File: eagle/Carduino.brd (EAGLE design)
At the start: 92.5 x 92.5 mm, 81 parts, among them IC1 DS3231M+TRL, IC2 FT232RL, IC3 SN74HCS596DR, IC4 SN74HCS596DR, IC5 SN74HCS596DR, IC6 SN74HCS596DR, IC8 ATTINY404-SSNR, U1 BAT-HLD-012-SMT

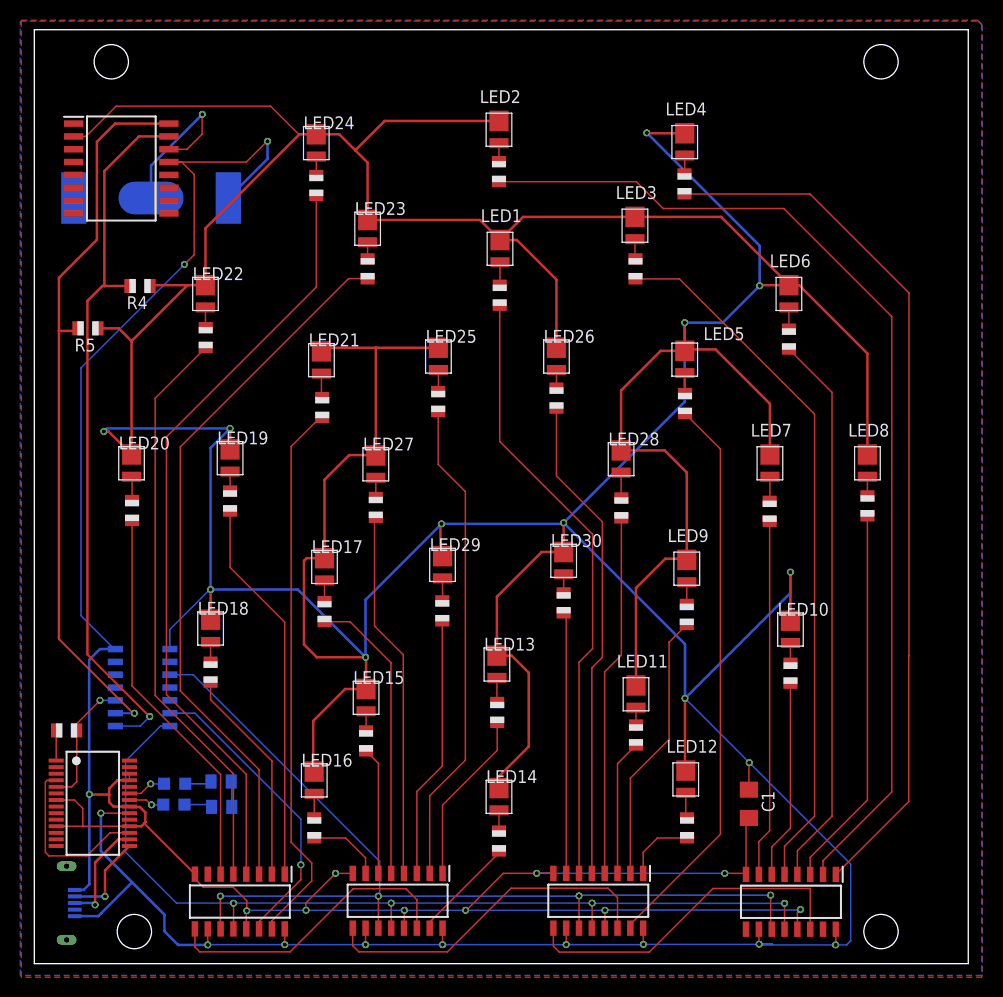
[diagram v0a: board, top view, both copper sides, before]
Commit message: added logo and moved USB port
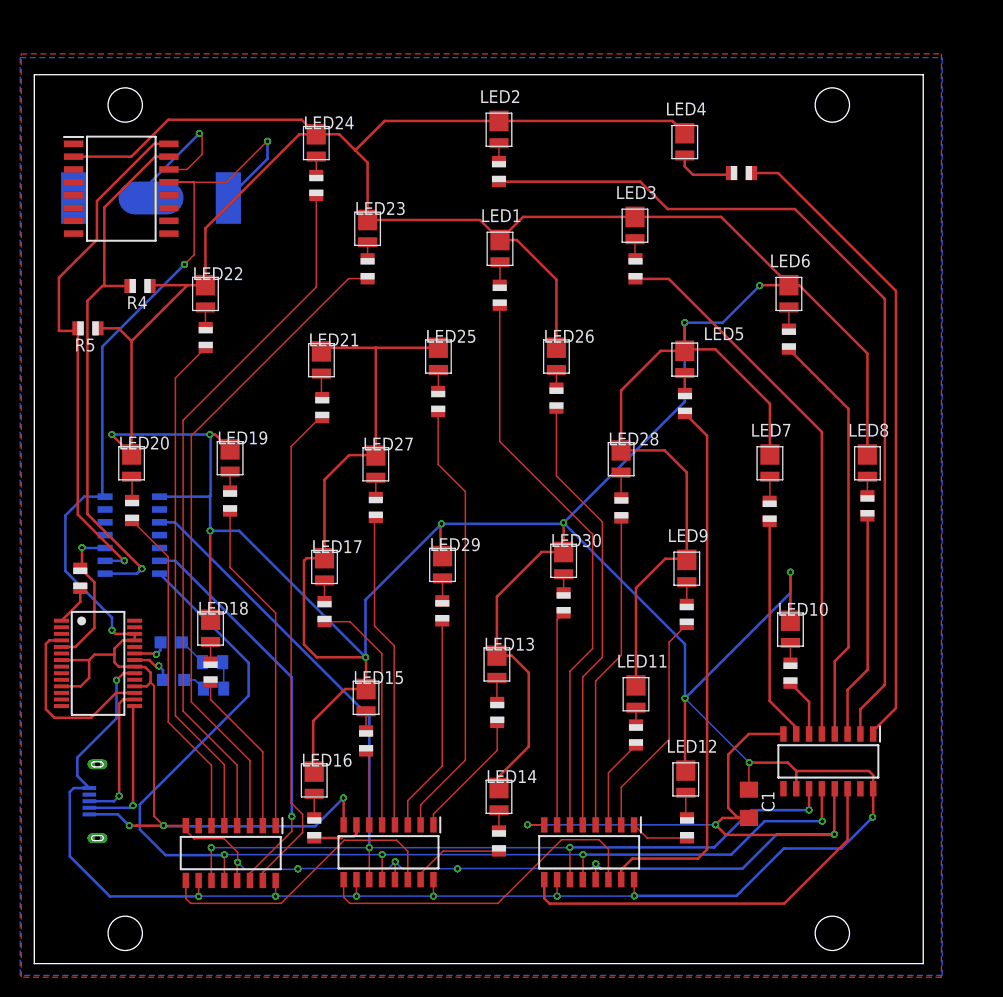
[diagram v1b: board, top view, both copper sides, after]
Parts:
- moved R1 15.1 mm to (4.55, 38.2), turned to 90 degrees
- moved IC8 15.1 mm to (9.70, 42.4)
- moved IC3 14.4 mm to (78.6, 20.0)
- moved TX 14.0 mm to (13.6, 31.8)
- moved IC2 13.9 mm to (6.31, 29.7)
- moved RX 12.3 mm to (13.8, 28.1)
- moved R3 11.8 mm to (17.7, 29.8)
- moved R2 11.7 mm to (17.8, 27.2)
- moved U$5 10.2 mm to (5.45, 16.1), turned to 270 degrees
- moved U$4 6.45 mm to (79.0, 85.0)
- moved R15 5.75 mm to (70.0, 78.3), turned to 0 degrees
- moved IC6 4.88 mm to (19.4, 10.9)
- moved IC4 4.88 mm to (54.9, 11.0)
- moved IC5 4.88 mm to (35.1, 11.0)
- moved U$2 4.82 mm to (79.0, 3.00)
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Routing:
- net GND: track 246.4 -> 273.6 mm, vias 12 -> 14
- net N$53: track 86.8 -> 63.9 mm
- net N$97: track 92.4 -> 114.2 mm
- net N$32: track 73.0 -> 52.7 mm
- net N$31: track 71.5 -> 53.7 mm
- net N$59: track 70.1 -> 54.6 mm
- net N$57: track 37.8 -> 22.4 mm
- net N$56: track 102.5 -> 87.1 mm
- net N$96: track 99.4 -> 114.2 mm
- net N$58: track 55.2 -> 41.1 mm
- net N$60: track 19.7 -> 5.78 mm
- net N$61: track 35.4 -> 22.1 mm
- net N$98: track 29.9 -> 39.7 mm
- net N$87: track 57.4 -> 50.6 mm
- net N$88: track 76.6 -> 70.1 mm
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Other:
- board size 92.5 x 92.5 mm -> 88 x 88 mm
- board text added: "C:/Users/pierr/Documents/Sparkle/vanillalogo.bmp"

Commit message: added realtime clock
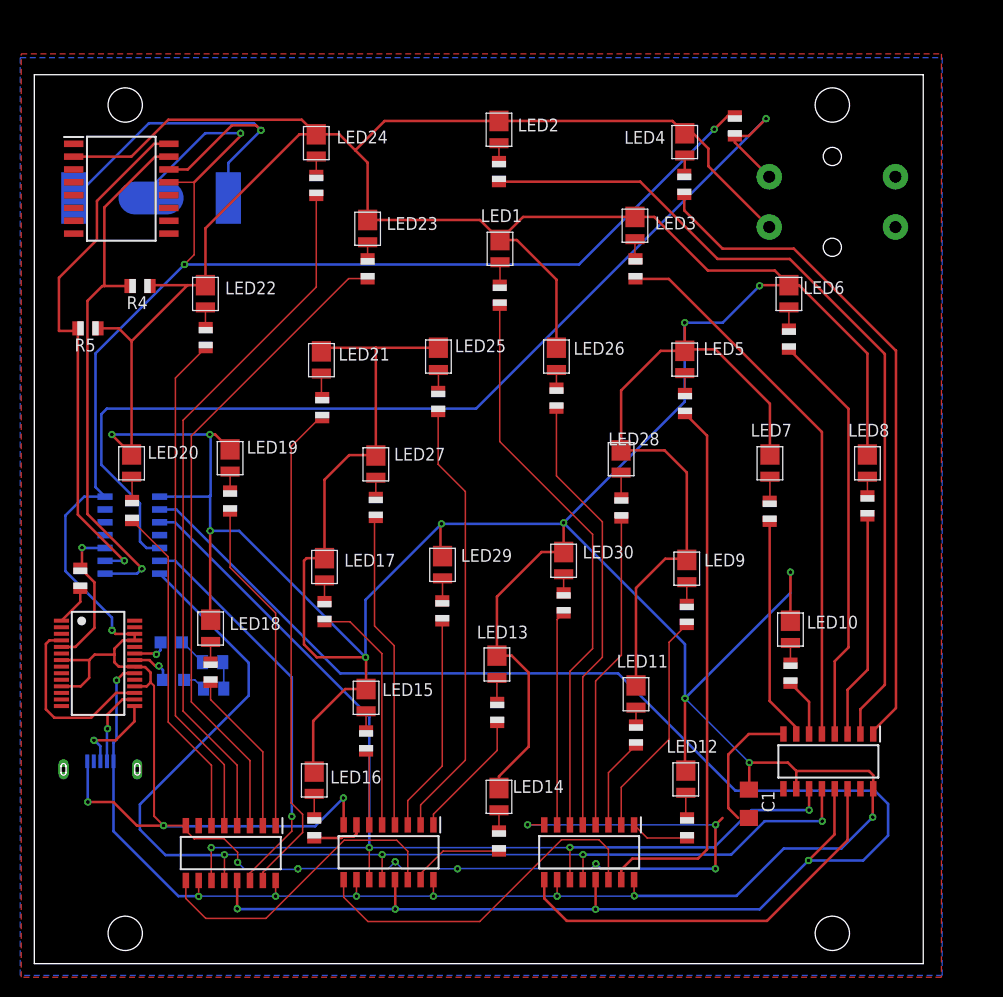
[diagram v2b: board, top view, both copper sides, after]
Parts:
- added R6: 4.7K, adafruit:R0805
- added S1: (no value), adafruit:B3F-40XX-ROUND
- moved R15 5.78 mm to (64.3, 77.1), turned to 270 degrees
- moved U$5 4.10 mm to (6.54, 20.0), turned to 0 degrees
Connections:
- new net N$34: IC8.5, R6.1, S1.2
- new net N$35: IC3.13, IC4.13, IC5.13, IC6.13, IC8.2
- net GND: now also R6.2; no longer IC3.13, IC4.13, IC5.13, IC6.13
- net N$100: now also U$5.3; no longer U$5.4
- net N$33: now also U1.VCC2
- net N$99: now also U$5.2; no longer U$5.3
- net VCC: now also S1.4
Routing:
- net N$35: track 0.00 -> 171.6 mm, vias 0 -> 4
- net N$34: track 0.00 -> 103.6 mm, vias 0 -> 1
- net GND: track 273.6 -> 305.3 mm, vias 14 -> 15
- net N$33: track 14.6 -> 41.1 mm
- net N$99: track 14.0 -> 7.97 mm
- net N$100: track 14.3 -> 8.74 mm
- net N$1: track 6.12 -> 1.88 mm
- net VCC: track 694.7 -> 698.8 mm
- net N$53: track 63.9 -> 67.2 mm
- net N$56: track 87.1 -> 83.9 mm
- net N$94: track 34.2 -> 35.7 mm
- net N$95: track 39.8 -> 41.2 mm
- net N$93: track 29.8 -> 31.0 mm

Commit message: better use of button to adjust dots
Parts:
- added C2: 4.7uF, resistor:C1206
- added C3: 1uF, resistor:C1206
- added CHARGING: Red, adafruit:CHIP-LED0805
- added CN1: (no value), adafruit:JST-PH-2-SMT-RA
- added IC7: NTMD4184PFR2G, SamacSys_Parts:SOIC127P600X175-8N
- added IC9: MCP73831T-3ACI_OT, SamacSys_Parts:SOT95P270X145-5N
- added R16: 470, adafruit:R0805
- added R21: 100K, adafruit:R0805
- added R22: 10K, adafruit:R0805
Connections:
- removed net +5V: R2.1, R3.1
- new net N$36: IC7.1, IC7.4, R21.1
- new net N$37: IC9.5, R22.1
- new net N$38: C2.1, CN1.1, IC7.5, IC9.3
- new net N$39: CHARGING.C, IC9.1
- new net N$40: CHARGING.A, R16.1
- net GND: now also C2.2, C3.1, CN1.2, IC9.2, R21.2, R22.2
- net VCC: now also C3.2, IC7.3, IC7.8, IC9.4, R16.2, R2.1, R3.1
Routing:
- net VCC: track 698.8 -> 793.2 mm, vias 19 -> 21
- net GND: track 305.3 -> 358.1 mm, vias 15 -> 16
- net N$38: track 0.00 -> 16.0 mm
- net N$36: track 0.00 -> 12.3 mm
- net N$97: track 114.2 -> 123.8 mm
- net N$37: track 0.00 -> 2.83 mm
- net +5V: track 2.66 -> 0.00 mm
- net N$39: track 0.00 -> 2.24 mm
- net N$33: track 41.1 -> 43.1 mm
- net N$40: track 0.00 -> 1.95 mm
- net N$98: track 39.7 -> 41.5 mm
